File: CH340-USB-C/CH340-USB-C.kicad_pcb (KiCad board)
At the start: 2 copper layers, 37.2 x 17.8 mm, 19 parts, among them J1 USB_C_Receptacle_USB2.0, J2 Conn_01x04_MountingPin, SW1 SW_Push_SPDT, U1 XC6206PxxxMR, U2 CH340N

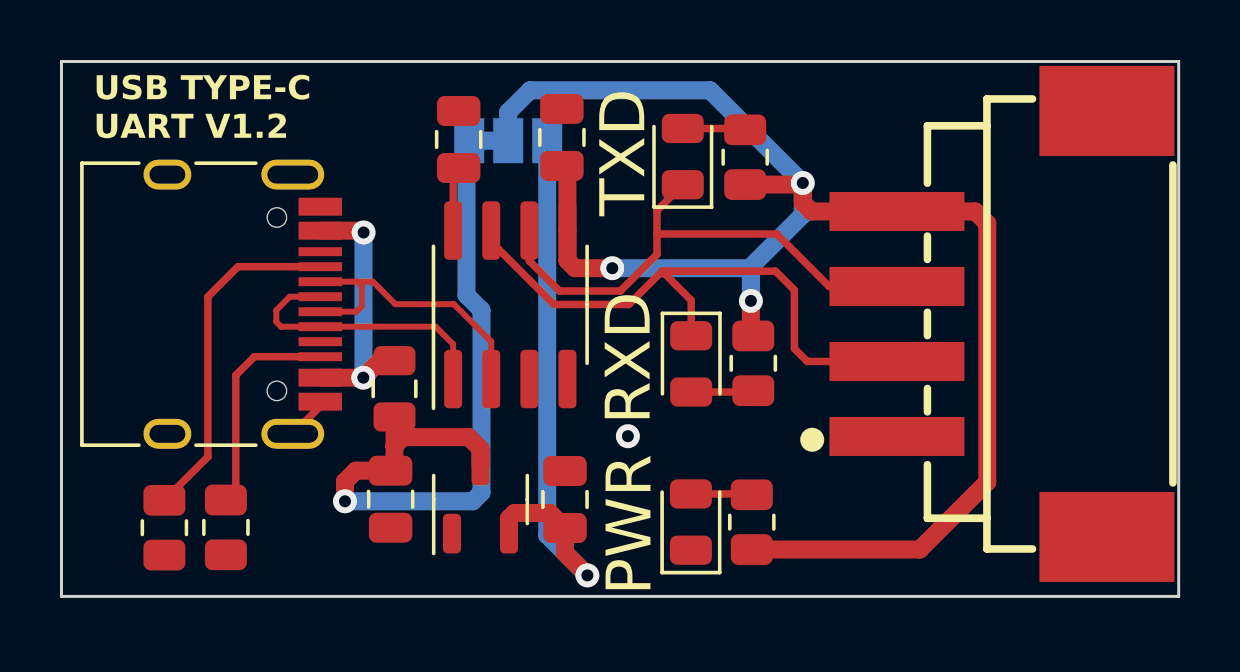
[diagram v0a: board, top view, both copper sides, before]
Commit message: 新增
1.可以選擇是否輸出電源(預設"不輸出")
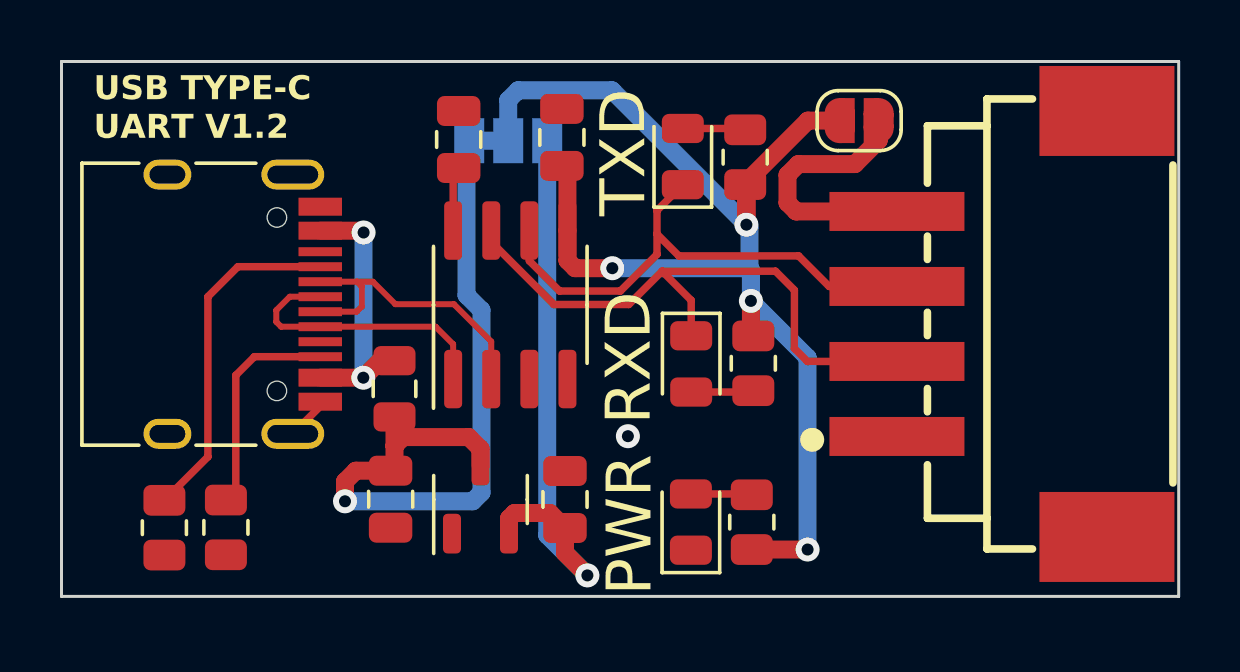
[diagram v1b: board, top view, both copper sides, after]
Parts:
- added JP1: Jumper_2_Open, Jumper:SolderJumper-2_P1.3mm_Open_RoundedPad1.0x1.5mm, F.Cu at (89.5, 90.4)
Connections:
- J2 pad 4: VCC -> Net-(J2-Pin_4)
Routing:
- net VCC: track 54.1 -> 42.2 mm, vias 3 -> 4
- net Net-(J2-Pin_4): track 0.00 -> 8.87 mm

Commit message: Update CH340-USB-C.kicad_pcb
將電源輸出選擇改到底層
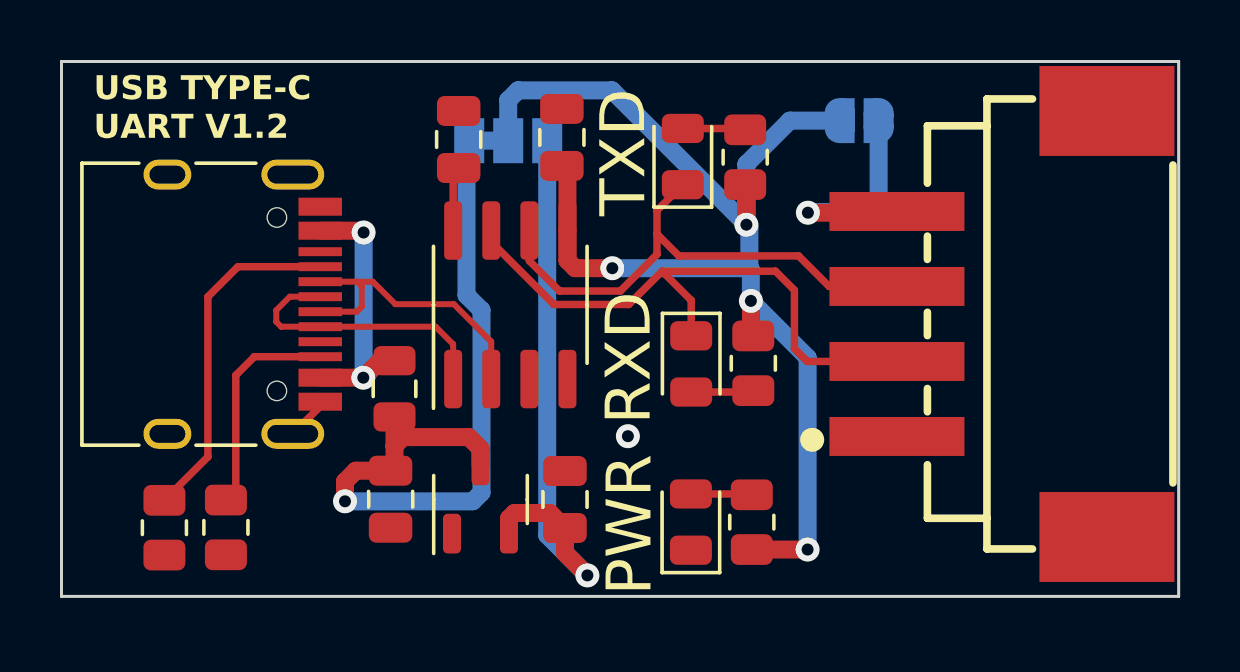
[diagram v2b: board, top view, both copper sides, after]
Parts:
- JP1: moved to B.Cu
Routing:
- net Net-(J2-Pin_4): track 8.87 -> 8.24 mm, vias 0 -> 1
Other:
- board text added: "Power out"
